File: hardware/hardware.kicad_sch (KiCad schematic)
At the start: 22 parts, among them U1 ESP32-C3-MINI-1U

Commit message: add thermocouple and zcd
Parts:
- added D?: LED, symbol Device:LED_Small
- added D?: PWR, symbol Device:LED_Small
- added J?: therm0, symbol Connector_Generic:Conn_01x02
- added J?: therm1, symbol Connector_Generic:Conn_01x02
- added R? (x2): 1k, symbol Device:R_Small
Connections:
- net +5V: now also R?.1
- net GND: now also D?.1 (K), D?.1 (K)
- net SCK: now reaches U1.12 (GPIO0/ADC1_CH0/XTAL_32K_P)
- net CS0: now reaches U1.13 (GPIO1/ADC1_CH1/XTAL_32K_N)
- net CS1: now reaches U1.16 (GPIO10)
- net HEAT0: now reaches U1.18 (GPIO4/ADC1_CH4)
- net HEAT1: now reaches U1.19 (GPIO5/ADC2_CH0)
- net LED: now reaches U1.20 (GPIO6)
- net LED: now also R?.1
- net ZCD: now reaches U1.21 (GPIO7)
- net MISO: now reaches U1.6 (GPIO3/ADC1_CH3)
- new net: D?.2 (A), R?.2 (x2)
- new net thermocouple0/T+: J?.2 (Pin_2)
- new net thermocouple0/T-: J?.1 (Pin_1)
- new net thermocouple1/T+: J?.2 (Pin_2)
- new net thermocouple1/T-: J?.1 (Pin_1)
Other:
- added sheet ZCD (ZCD.kicad_sch)
- added sheet thermocouple0 (thermocouple.kicad_sch)
- added sheet thermocouple1 (thermocouple.kicad_sch)
- note added: "TODO move as needed"
- moved on the sheet: C?, R?, SW?

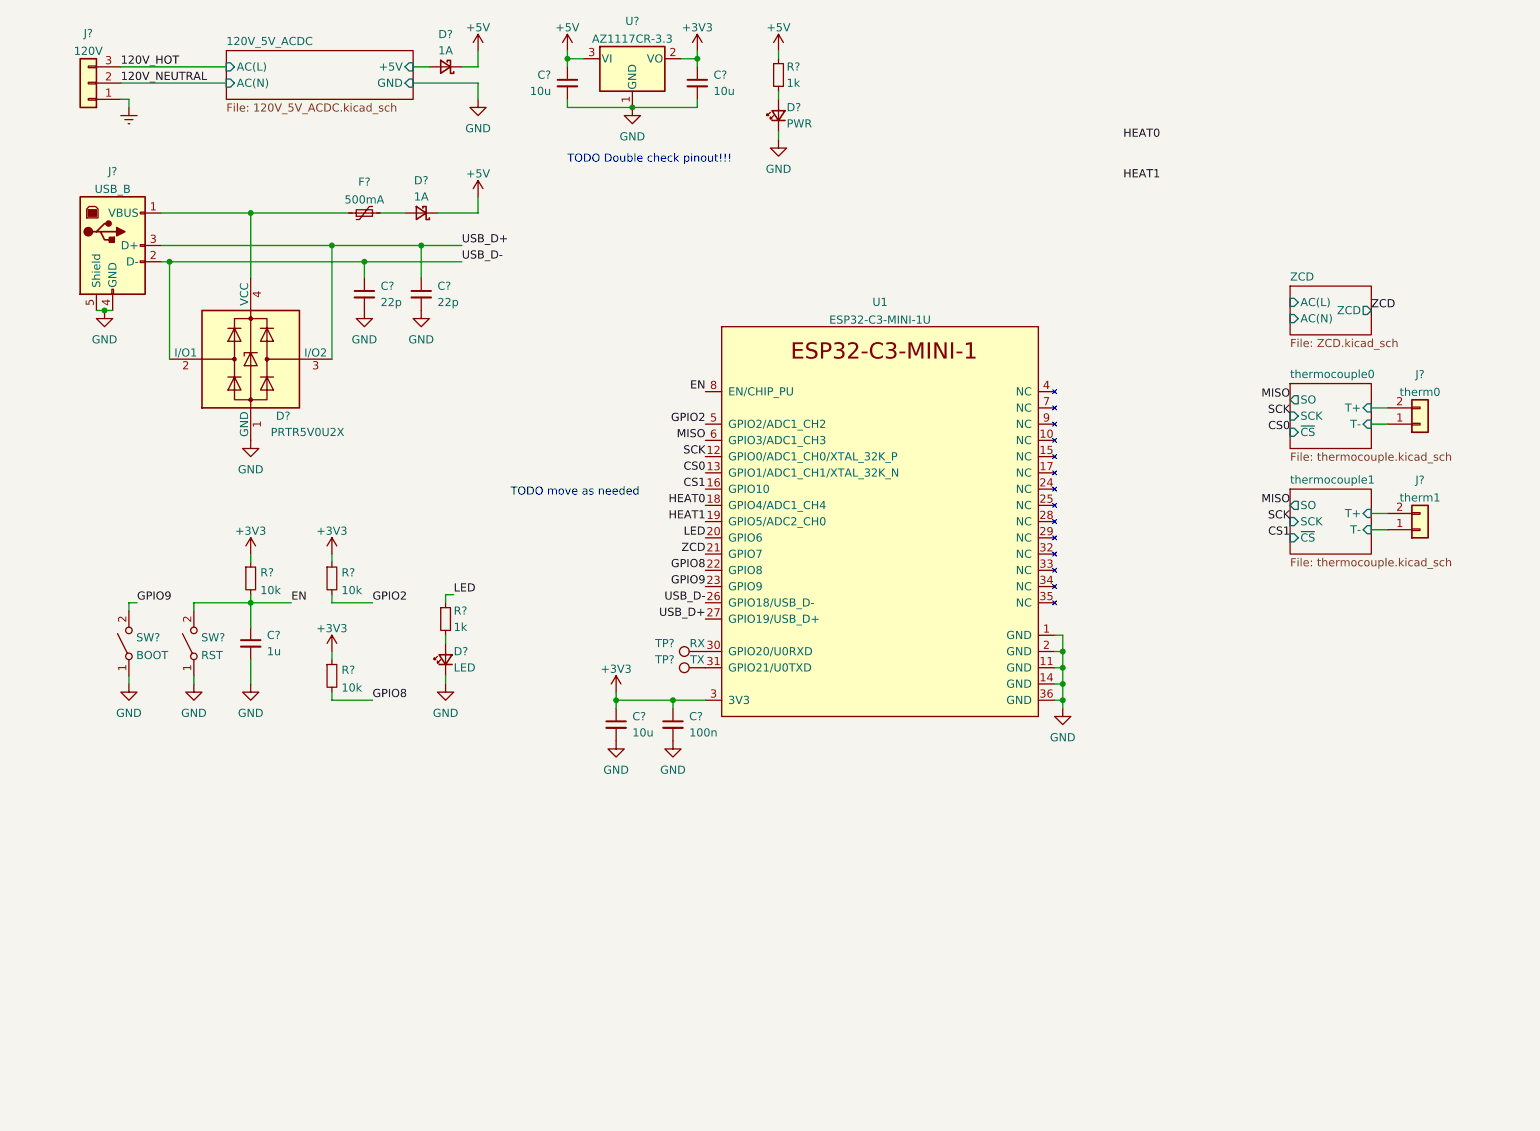
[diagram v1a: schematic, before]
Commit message: added heater
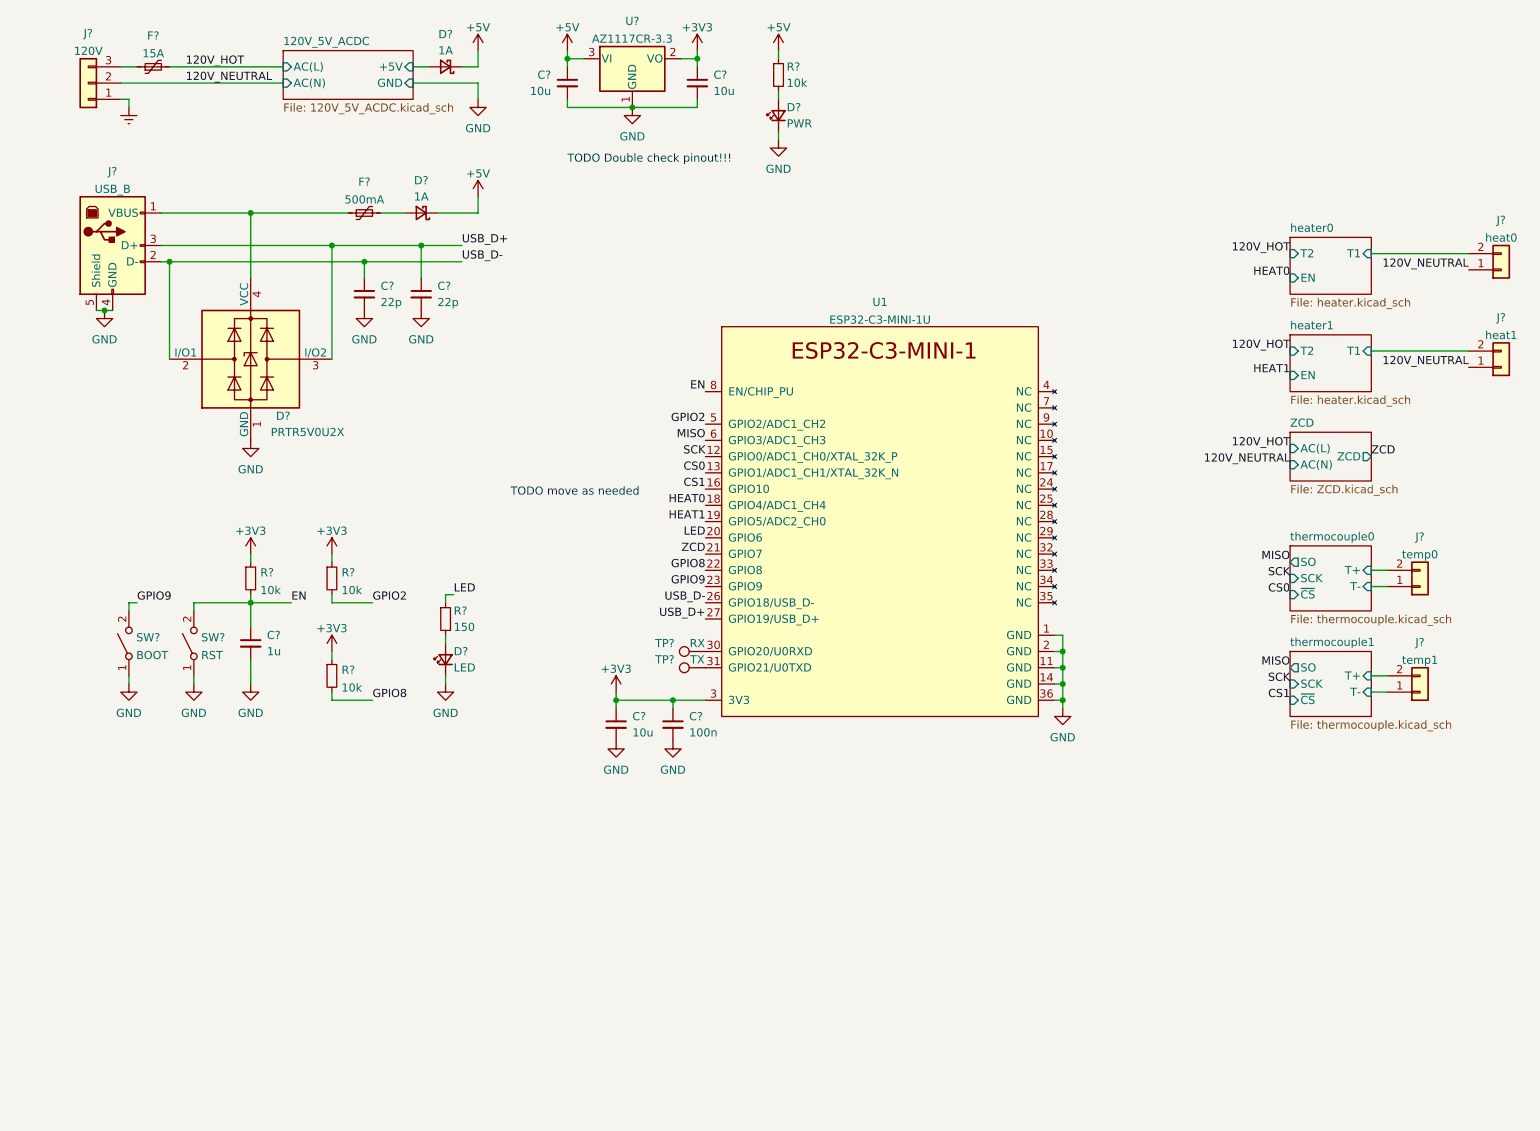
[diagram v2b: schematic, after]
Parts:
- added F?: 15A, symbol Device:Polyfuse_Small
- added J?: heat1, symbol Connector_Generic:Conn_01x02
- added J?: heat0, symbol Connector_Generic:Conn_01x02
- J?: value therm0 -> temp0
- J?: value therm1 -> temp1
- R?: value 1k -> 10k
- R?: value 1k -> 150
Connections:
- net 120V_HOT: now also F?.2; no longer J?.3 (Pin_3)
- net 120V_NEUTRAL: now also J?.1 (Pin_1), J?.1 (Pin_1)
- new net: F?.1, J?.3 (Pin_3)
- new net heater0/T1: J?.2 (Pin_2)
- new net heater1/T1: J?.2 (Pin_2)
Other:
- added sheet heater0 (heater.kicad_sch)
- added sheet heater1 (heater.kicad_sch)
- moved on the sheet: J?

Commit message: assigned footprints
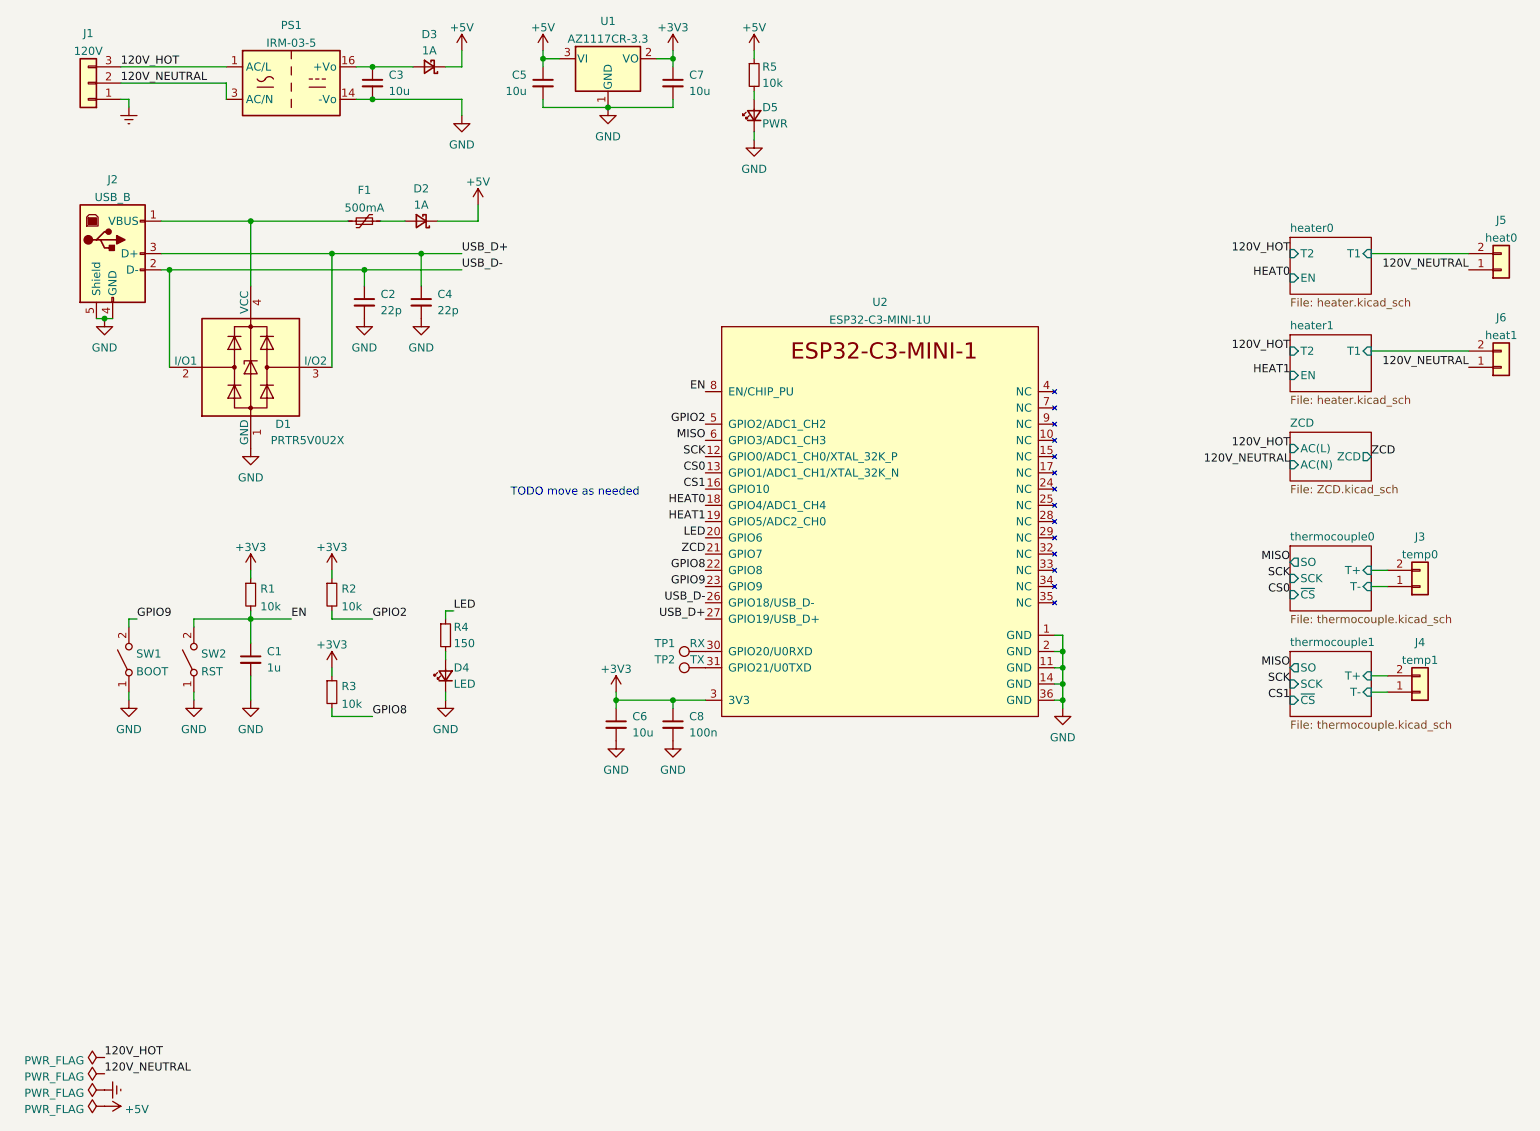
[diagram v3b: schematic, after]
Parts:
- removed F?: 15A, symbol Device:Polyfuse_Small
- added C3: 10u, Capacitor_SMD:C_0805_2012Metric, symbol Device:C_Small
- added PS1: IRM-03-5, Converter_ACDC:Converter_ACDC_MeanWell_IRM-03-xx_THT, symbol Converter_ACDC:IRM-03-5
- C1, C2, C4, C8: renamed from C?; footprint (none) -> Capacitor_SMD:C_0603_1608Metric
- C5, C6, C7: renamed from C?; footprint (none) -> Capacitor_SMD:C_0805_2012Metric
- D2, D3: renamed from D?; footprint (none) -> Diode_SMD:D_SOD-123F
- D4, D5: renamed from D?; footprint (none) -> LED_SMD:LED_0603_1608Metric
- F1: renamed from F?; footprint (none) -> Fuse:Fuse_1206_3216Metric
- J1: renamed from J?; footprint (none) -> extraparts:Molex_MicroFit+_RH_1row_3pin
- J2: renamed from J?; footprint (none) -> Connector_USB:USB_B_TE_5787834_Vertical
- J3, J4: renamed from J?; footprint (none) -> extraparts:Molex_DuraClik_RH_2pin
- J5, J6: renamed from J?; footprint (none) -> extraparts:Molex_MicroFit+_RH_1row_2pin
- R1, R2, R3, R4, R5: renamed from R?; footprint (none) -> Resistor_SMD:R_0603_1608Metric
- SW1, SW2: renamed from SW?; footprint (none) -> Button_Switch_SMD:SW_SPST_PTS810
- TP1, TP2: renamed from TP?; footprint (none) -> TestPoint:TestPoint_Plated_Hole_D2.0mm
- U1: renamed from U?; footprint (none) -> Package_TO_SOT_SMD:SOT-89-3
- gave numbers to parts that had none: 1
- renumbered U1 to U2
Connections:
- net 120V_HOT: now also J1.3 (Pin_3), PS1.1 (AC/L)
- net 120V_NEUTRAL: now also PS1.3 (AC/N)
- net GND: now also C3.2, PS1.14 (-Vo)
- net 120V_5V_ACDC/+5V: no longer names the net of D3.2 (A)
- net 120V_5V_ACDC/+5V: now also C3.1, PS1.16 (+Vo)
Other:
- removed sheet 120V_5V_ACDC
- note removed: "TODO Double check pinout!!!"
- moved on the sheet: C1, C2, C4, C5, C7, D1, D2, D3, D4, D5, F1, J2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
